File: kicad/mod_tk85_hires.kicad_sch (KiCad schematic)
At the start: 23 parts, among them IC2_PINS_13_24 IC2 pinos 13-24, IC2_PINS_1_12 IC2 pinos 1-12, J1 Sinais do TK-85, U1 6116, U2 6116, U3 6116, U4 2364 (IC2), U5 74LS93, U6 74LS93, U7 74LS157, U8 74LS138, U9 74LS00

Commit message: Ajustes de revisão do esquema (rev 2)
Correções apontadas na revisão visual:

- PWR_FLAGs soltos no canto inferior esquerdo removidos; agora ficam
  presos aos stubs de entrada de alimentação do interposer (pino 1 =
  +5V, pino 12 = GND), onde a energia realmente entra vinda do TK-85
- J1 (Sinais do TK-85) movido para dentro da folha — os labels
  ultrapassavam a borda direita do A3
- Legendas soltas consolidadas num bloco NOTAS no canto superior
  direito (área livre), eliminando sobreposição com U9E e RV1
- Notas reescritas como descrição do projeto, sem justificar
  correções históricas; carimbo aponta docs/correcoes-errata.md
- Reference/Value de símbolos com pinos verticais (C1-C10, RV1)
  deslocados para o lado, fora do fio

Verificação: netlist idêntica (46 nets pretendidas conferem
exatamente), ERC 0 erros / 0 avisos, PDF e SVG reexportados.

Co-Authored-By: Claude Fable 5 <noreply@anthropic.com>
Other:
- note added: "1. Interposer: encaixa no soquete do IC2 (ROM de caracteres) do TK-85. CS_ROM = pino 20 do IC2."
- note added: "2. 6116: /WE = WR do Z80 (pino 22), /OE = GND, /CS0../CS2 vindos do 74LS138."
- note added: "3. 74LS157 seleciona o endereco: CPU quando RFSH=1, contador de video quando RFSH=0."
- note added: "4. RV1 (reostato: cursor ligado a um extremo) ajusta o reset dos contadores."
- note added: "NOTAS"
- note removed: "6116: /WE = WR do Z80 (pino 22), /OE = GND (errata). /CS0..2 vem do 74LS138."
- note removed: "74LS157 seleciona o endereco: CPU quando RFSH=1, contador de video quando RFSH=0."
- note removed: "CS_ROM = pino 20 do IC2, agora ligado a ROM (correcao vs. projeto anterior)."
- note removed: "Interposer: encaixa no soquete do IC2 (ROM de caracteres) do TK-85."
- note removed: "RV1 (errata): ajusta o reset dos contadores. Cursor e extremo ligados juntos."

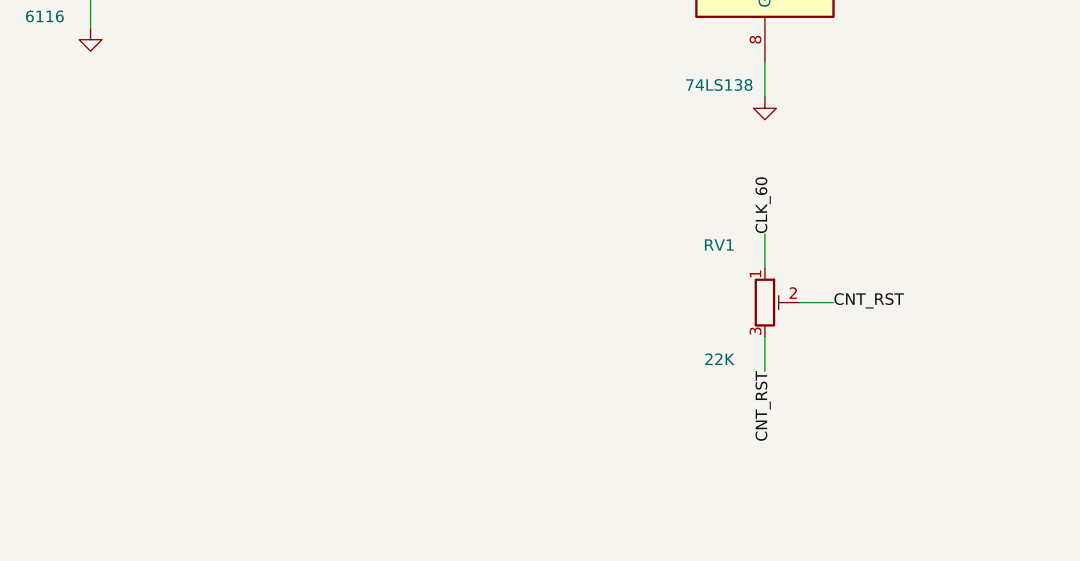
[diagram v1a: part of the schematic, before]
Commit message: Afasta RV1 do carimbo da folha
Movido de x=300 para x=240 (área livre abaixo do 74LS138), a pedido
da revisão. Netlist idêntica, ERC 0/0, PDF e SVG reexportados.

Co-Authored-By: Claude Fable 5 <noreply@anthropic.com>
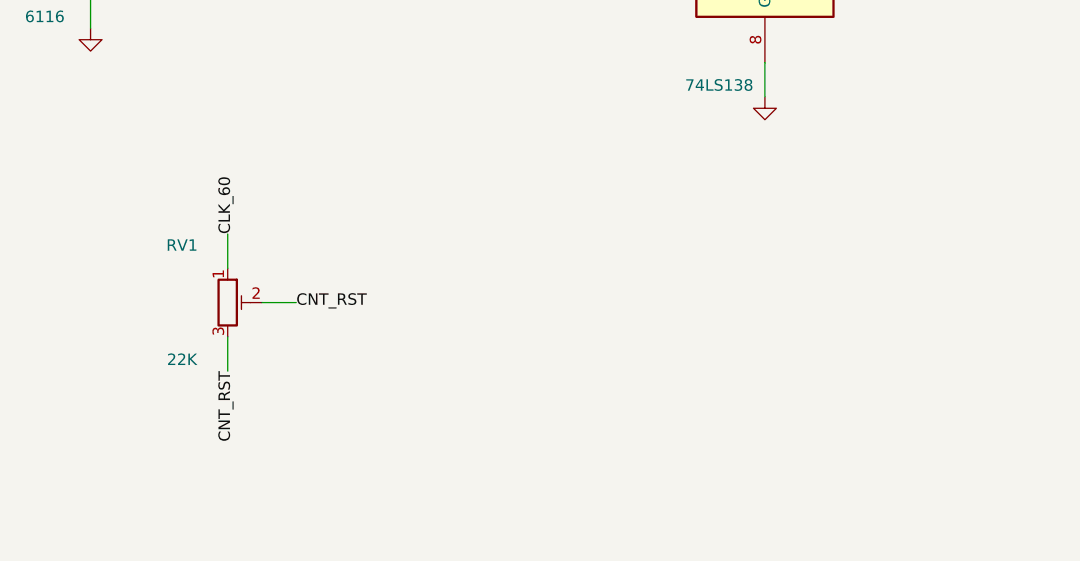
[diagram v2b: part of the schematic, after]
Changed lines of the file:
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@@
 	(symbol
 		(lib_id "Device:R_Potentiometer_Trim")
-		(at 299.72 234.95 0)
+		(at 240.03 234.95 0)
 		(unit 1)
 		(exclude_from_sim no)
@@
 		(dnp no)
 		(property "Reference" "RV1"
-			(at 294.64 228.6 0)
+			(at 234.95 228.6 0)
 			(effects
 				(font
@@
 		)
 		(property "Value" "22K"
-			(at 294.64 241.3 0)
+			(at 234.95 241.3 0)
 			(effects
 				(font
@@
 		)
 		(property "Footprint" "Potentiometer_THT:Potentiometer_Bourns_3266P_Horizontal"
-			(at 299.72 234.95 0)
+			(at 240.03 234.95 0)
 			(effects
 				(font
@@
 		)
 		(property "Datasheet" ""
-			(at 299.72 234.95 0)
+			(at 240.03 234.95 0)
 			(effects
 				(font
@@
 	(wire
 		(pts
-			(xy 299.72 231.14) (xy 299.72 227.33)
+			(xy 240.03 231.14) (xy 240.03 227.33)
 		)
 		(stroke
@@
 	)
 	(label "CLK_60"
-		(at 299.72 227.33 90)
+		(at 240.03 227.33 90)
 		(effects
 			(font
@@
 	(wire
 		(pts
-			(xy 303.53 234.95) (xy 307.34 234.95)
+			(xy 243.84 234.95) (xy 247.65 234.95)
 		)
 		(stroke
@@
 	)
 	(label "CNT_RST"
-		(at 307.34 234.95 0)
+		(at 247.65 234.95 0)
 		(effects
 			(font
@@
 	(wire
 		(pts
-			(xy 299.72 238.76) (xy 299.72 242.57)
+			(xy 240.03 238.76) (xy 240.03 242.57)
 		)
 		(stroke
@@
 	)
 	(label "CNT_RST"
-		(at 299.72 242.57 90)
+		(at 240.03 242.57 90)
 		(effects
 			(font

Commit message: PCB: contorno em T medido sobre o TK-85 e posicionamento completo
Contorno ancorado no soquete do IC2 (foto da placa calibrada em
10 px/mm pelo passo dos DIPs; conferida no DIP-40 do Z80):

- Língua x -10,5..+10 / y -20..+17,5 sobre o IC2, com os dois pentes
  do interposer (pino 1 ao norte, casando com o IC2), U9 e U6
- Corpo x -70..+35,6 / y +17,5..+59 sobre as fileiras planas de
  TTL/RAM; recorte SE desvia do capacitor de tântalo
- Fora do contorno: capacitor azul deitado, 2716+soquete, Z80
- J1 na borda sul com pinos para a frente (fios voadores)
- Footprints corrigidos no esquema: DIP-14/16 de 7,62 mm (eram
  10,16 mm) e variantes _Socket; netlist re-verificada (idêntica)
- DRC: 0 violações físicas (courtyard/borda); restam 161 itens não
  conectados = ratsnest, roteamento é a próxima etapa
- docs/mecanica.md: obstáculos altos medidos e exigência de DOIS
  níveis de soquete torneado no interposer (ICs 30-37 soquetados,
  ~8-9,5 mm sob a placa; vão de 1 nível = ~6-7 mm não passa)

Gerado por script (netlist -> footprints das libs oficiais com
verificador de colisão/contenção de courtyards).

Co-Authored-By: Claude Fable 5 <noreply@anthropic.com>
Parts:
- U1, U2, U3, U4: footprint Package_DIP:DIP-24_18.0mmx34.29mm_W15.24mm_LongPads -> Package_DIP:DIP-24_W15.24mm_Socket
- U5, U6, U9: footprint Package_DIP:DIP-14_W10.16mm -> Package_DIP:DIP-14_W7.62mm_Socket
- U7, U8: footprint Package_DIP:DIP-16_W10.16mm -> Package_DIP:DIP-16_W7.62mm_Socket
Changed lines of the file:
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@@
 			)
 		)
-		(property "Footprint" "Package_DIP:DIP-24_18.0mmx34.29mm_W15.24mm_LongPads"
+		(property "Footprint" "Package_DIP:DIP-24_W15.24mm_Socket"
 			(at 149.86 77.47 0)
 			(effects
@@
 			)
 		)
-		(property "Footprint" "Package_DIP:DIP-24_18.0mmx34.29mm_W15.24mm_LongPads"
+		(property "Footprint" "Package_DIP:DIP-24_W15.24mm_Socket"
 			(at 149.86 175.26 0)
 			(effects
@@
 			)
 		)
-		(property "Footprint" "Package_DIP:DIP-24_18.0mmx34.29mm_W15.24mm_LongPads"
+		(property "Footprint" "Package_DIP:DIP-24_W15.24mm_Socket"
 			(at 224.79 77.47 0)
 			(effects
@@
 			)
 		)
-		(property "Footprint" "Package_DIP:DIP-24_18.0mmx34.29mm_W15.24mm_LongPads"
+		(property "Footprint" "Package_DIP:DIP-24_W15.24mm_Socket"
 			(at 224.79 175.26 0)
 			(effects
@@
 			)
 		)
-		(property "Footprint" "Package_DIP:DIP-16_W10.16mm"
+		(property "Footprint" "Package_DIP:DIP-16_W7.62mm_Socket"
 			(at 299.72 91.44 0)
 			(effects
@@
 			)
 		)
-		(property "Footprint" "Package_DIP:DIP-16_W10.16mm"
+		(property "Footprint" "Package_DIP:DIP-16_W7.62mm_Socket"
 			(at 299.72 190.5 0)
 			(effects
@@
 			)
 		)
-		(property "Footprint" "Package_DIP:DIP-14_W10.16mm"
+		(property "Footprint" "Package_DIP:DIP-14_W7.62mm_Socket"
 			(at 369.57 73.66 0)
 			(effects
@@
 			)
 		)
-		(property "Footprint" "Package_DIP:DIP-14_W10.16mm"
+		(property "Footprint" "Package_DIP:DIP-14_W7.62mm_Socket"
 			(at 369.57 139.7 0)
 			(effects
@@
 			)
 		)
-		(property "Footprint" "Package_DIP:DIP-14_W10.16mm"
+		(property "Footprint" "Package_DIP:DIP-14_W7.62mm_Socket"
 			(at 54.61 218.44 0)
 			(effects
@@
 			)
 		)
-		(property "Footprint" "Package_DIP:DIP-14_W10.16mm"
+		(property "Footprint" "Package_DIP:DIP-14_W7.62mm_Socket"
 			(at 119.38 218.44 0)
 			(effects
@@
 			)
 		)
-		(property "Footprint" "Package_DIP:DIP-14_W10.16mm"
+		(property "Footprint" "Package_DIP:DIP-14_W7.62mm_Socket"
 			(at 54.61 255.27 0)
 			(effects
@@
 			)
 		)
-		(property "Footprint" "Package_DIP:DIP-14_W10.16mm"
+		(property "Footprint" "Package_DIP:DIP-14_W7.62mm_Socket"
 			(at 119.38 255.27 0)
 			(effects
@@
 			)
 		)
-		(property "Footprint" "Package_DIP:DIP-14_W10.16mm"
+		(property "Footprint" "Package_DIP:DIP-14_W7.62mm_Socket"
 			(at 185.42 255.27 0)
 			(effects

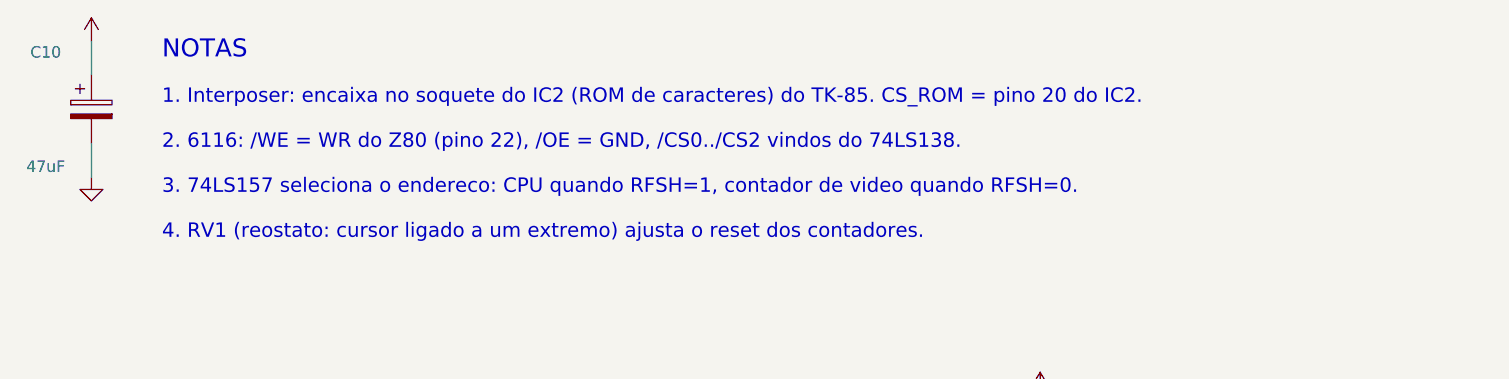
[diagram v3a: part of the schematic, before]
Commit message: Corrige a natureza do IC2 (ROM principal) e registra medição de altura
- IC2/2364 é a ROM PRINCIPAL do TK-85 (BASIC/sistema + tabelas de
  caracteres, como no ZX81), não uma "ROM de caracteres" dedicada.
  Corrigido em README, descrição do circuito, errata, referências,
  mecânica e na nota 1 do esquema (PDF/SVG reexportados; netlist
  idêntica, ERC 0/0)
- docs/mecanica.md: medição real do gabinete — ~12 mm livres acima
  da ROM (teto ~17 mm sobre a placa-mãe). A pilha de 2 níveis
  (~20-26 mm) está descartada; opções viáveis: 1 nível + soquete
  extra (vão ~10-11 mm, CIs do mod soldados) mantendo o contorno,
  ou 1 nível simples com contorno redesenhado fora dos ICs 30-37.
  Pendente: medir a folga sobre a região sul (lado do teclado)

Co-Authored-By: Claude Fable 5 <noreply@anthropic.com>
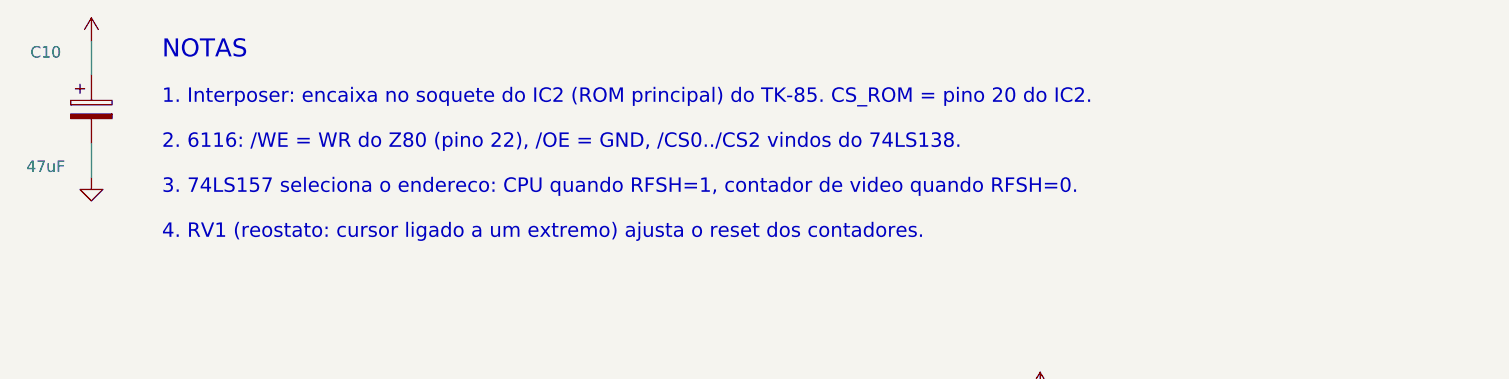
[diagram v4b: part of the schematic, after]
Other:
- note added: "1. Interposer: encaixa no soquete do IC2 (ROM principal) do TK-85. CS_ROM = pino 20 do IC2."
- note removed: "1. Interposer: encaixa no soquete do IC2 (ROM de caracteres) do TK-85. CS_ROM = pino 20 do IC2."
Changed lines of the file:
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@@
 		)
 	)
-	(text "1. Interposer: encaixa no soquete do IC2 (ROM de caracteres) do TK-85. CS_ROM = pino 20 do IC2."
+	(text "1. Interposer: encaixa no soquete do IC2 (ROM principal) do TK-85. CS_ROM = pino 20 do IC2."
 		(at 272 25 0)
 		(effects

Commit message: RV1 com ajuste por cima (3266W), silk do usuário e opção ROM-na-língua
- RV1 trocado de Bourns 3266P (lateral — parafuso ficava voltado
  para o interior da placa, inacessível) para 3266W (ajuste pelo
  topo), mantendo os pads 1/2 nas posições originais; /CS0 foi
  re-roteado para liberar o novo pad 3, e o courtyard embutido do
  footprint foi aparado 0,25 mm (corpos reais ficam ~1 mm afastados
  de U1/C9). DRC: 0 violações elétricas, 0 pads desconectados
- Ajustes manuais de silkscreen do usuário incluídos
- docs/mecanica.md: montagem da ROM diretamente sobre a língua do
  interposer (as nets dos pentes são idênticas às de U4, pino a
  pino) usando soquete DIP-24 torneado wire-wrap; U4 fica
  despopulado nessa opção. Nota sobre o RV1
- BOM atualizada (footprints _Socket/W7.62 corretos e 3266W);
  esquema com o campo de footprint do RV1 atualizado
- Gerbers, furação, zip e PDF da placa regenerados

Co-Authored-By: Claude Fable 5 <noreply@anthropic.com>
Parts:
- RV1: footprint Potentiometer_THT:Potentiometer_Bourns_3266P_Horizontal -> Potentiometer_THT:Potentiometer_Bourns_3266W_Vertical
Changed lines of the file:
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@@
 			)
 		)
-		(property "Footprint" "Potentiometer_THT:Potentiometer_Bourns_3266P_Horizontal"
+		(property "Footprint" "Potentiometer_THT:Potentiometer_Bourns_3266W_Vertical"
 			(at 240.03 234.95 0)
 			(effects
